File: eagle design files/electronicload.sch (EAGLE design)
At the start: 31 parts, among them Q1 IRLB3034PbF, U1 ARDUINO_BLUEPILL, U2 MCP6004-I/SL, X1 ED350/2

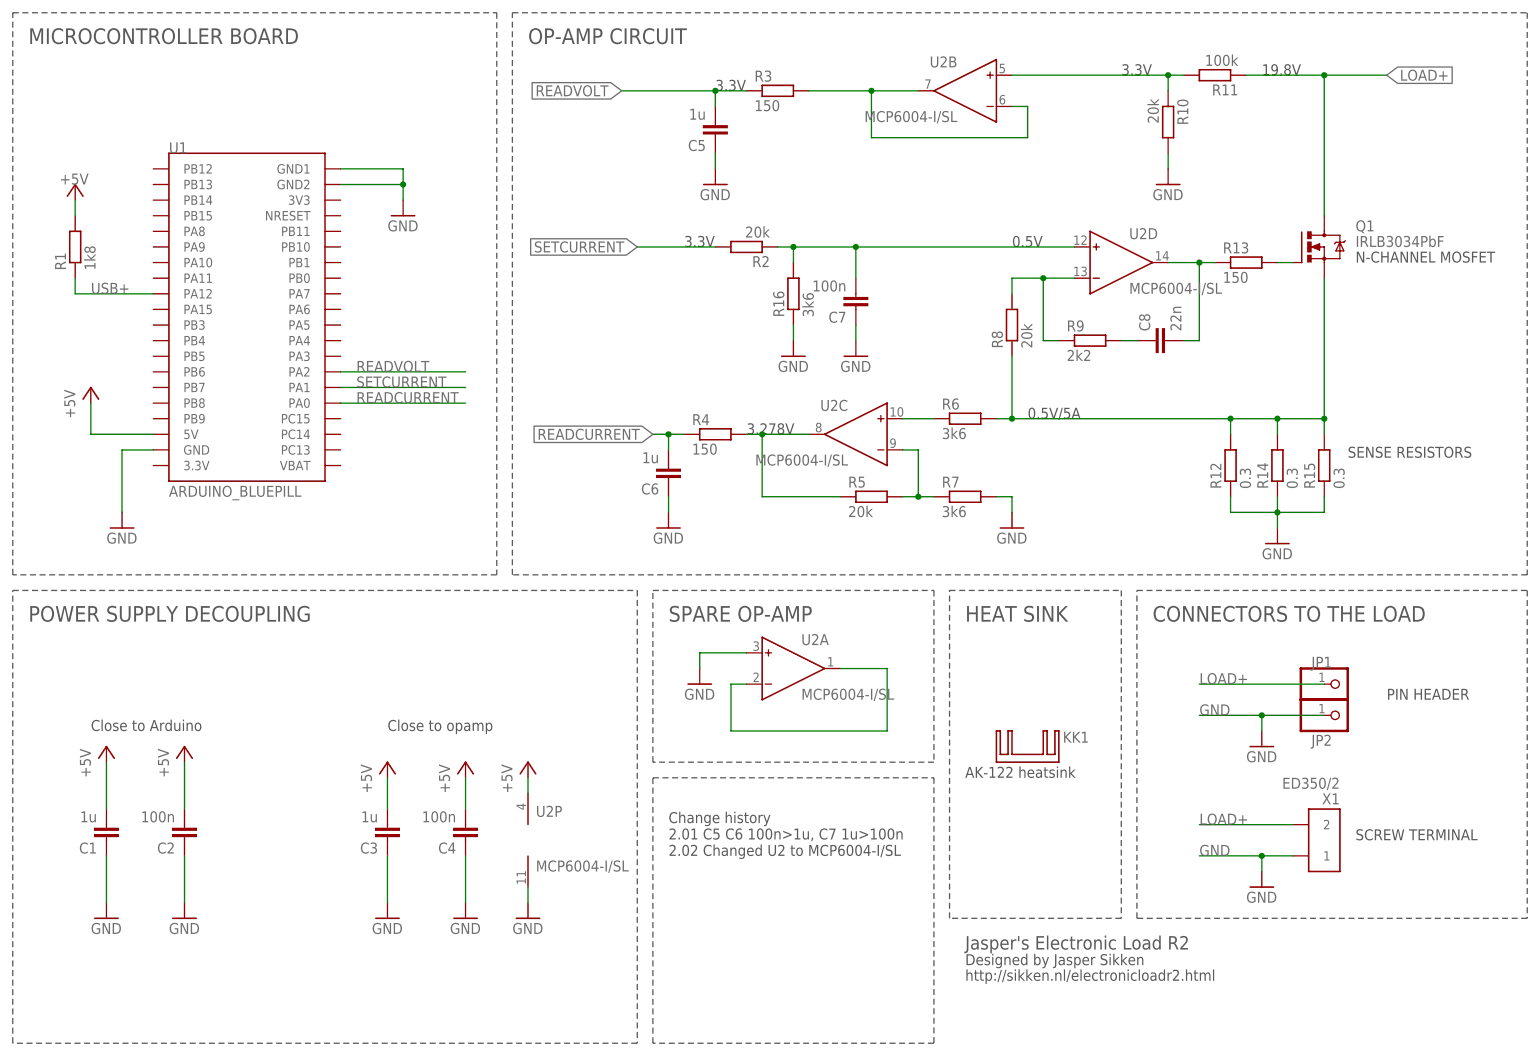
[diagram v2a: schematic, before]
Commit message: 2.03 Changed mosfet to the much more robust BTS133
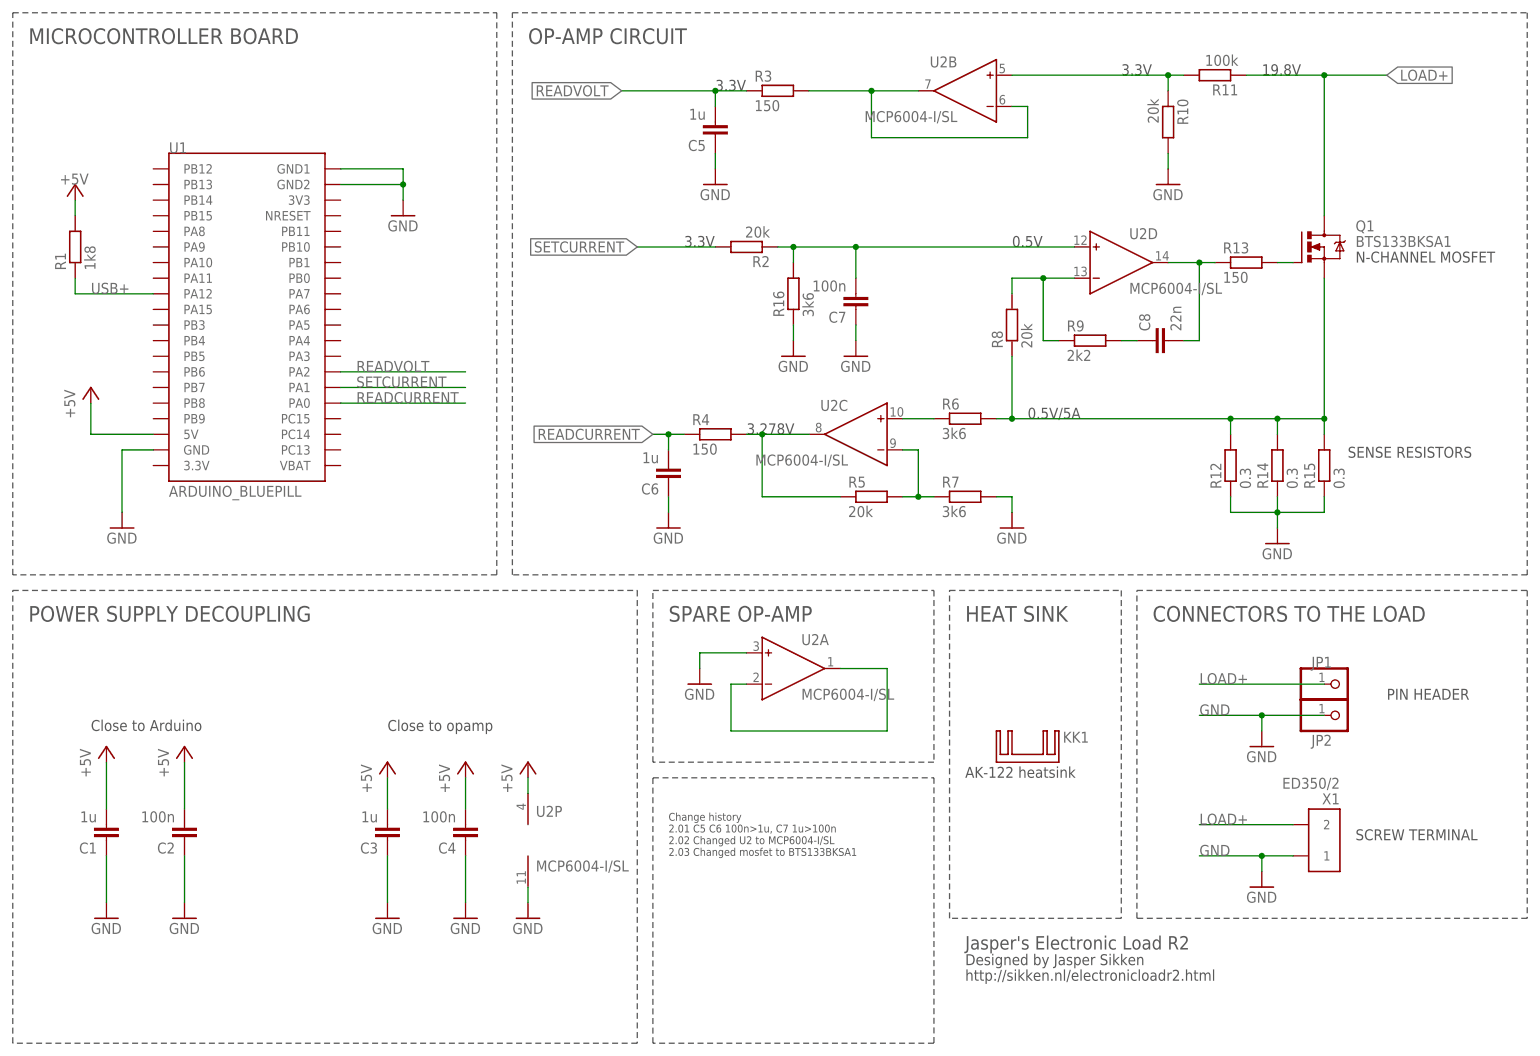
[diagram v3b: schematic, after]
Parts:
- Q1: value IRLB3034PbF -> BTS133BKSA1; DIGIKEY IRLB3034PbF -> BTS133BKSA1-ND; FARNELL_OC (none) -> 2480556; MOUSER_OC (none) -> 726-BTS133BKSA1
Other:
- note added: "Change history 2.01 C5 C6 100n>1u, C7 1u>100n 2.02 Changed U2 to MCP6004-I/SL 2.03 Changed mosfet to BTS133BKSA1"
- note removed: "Change history 2.01 C5 C6 100n>1u, C7 1u>100n 2.02 Changed U2 to MCP6004-I/SL"
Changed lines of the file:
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@@
 <part name="GND3" library="supply1" library_urn="urn:adsk.eagle:library:371" deviceset="GND" device=""/>
 <part name="GND1" library="supply1" library_urn="urn:adsk.eagle:library:371" deviceset="GND" device=""/>
-<part name="Q1" library="electronicload" deviceset="IRLZ44Z" device="" value="IRLB3034PbF">
-<attribute name="DIGIKEY" value="IRLB3034PbF"/>
+<part name="Q1" library="electronicload" deviceset="IRLZ44Z" device="" value="BTS133BKSA1">
+<attribute name="DIGIKEY" value="BTS133BKSA1-ND"/>
+<attribute name="FARNELL_OC" value="2480556"/>
+<attribute name="MOUSER_OC" value="726-BTS133BKSA1"/>
 </part>
 <part name="C5" library="rcl" library_urn="urn:adsk.eagle:library:334" deviceset="C-EU" device="C0603K" package3d_urn="urn:adsk.eagle:package:23680/2" value="1u">
@@
 <text x="162.56" y="48.26" size="1.778" layer="97">AK-122 heatsink</text>
 <text x="162.56" y="20.32" size="2.1844" layer="97">Jasper's Electronic Load R2</text>
-<text x="114.3" y="35.56" size="1.778" layer="97">Change history
+<text x="114.3" y="35.56" size="1.27" layer="97">Change history
 2.01 C5 C6 100n&gt;1u, C7 1u&gt;100n
-2.02 Changed U2 to MCP6004-I/SL</text>
+2.02 Changed U2 to MCP6004-I/SL
+2.03 Changed mosfet to BTS133BKSA1</text>
 <wire x1="111.76" y1="48.26" x2="157.48" y2="48.26" width="0.1524" layer="97" style="shortdash"/>
 <wire x1="157.48" y1="48.26" x2="157.48" y2="5.08" width="0.1524" layer="97" style="shortdash"/>
@@
 </instance>
 <instance part="GND1" gate="1" x="22.86" y="25.4"/>
-<instance part="Q1" gate="G$1" x="218.44" y="134.62"/>
+<instance part="Q1" gate="G$1" x="218.44" y="134.62">
+<attribute name="FARNELL_OC" x="218.44" y="134.62" size="1.778" layer="96" display="off"/>
+<attribute name="MOUSER_OC" x="218.44" y="134.62" size="1.778" layer="96" display="off"/>
+</instance>
 <instance part="C5" gate="G$1" x="121.92" y="152.4" rot="R180">
 <attribute name="DIGIKEY" x="121.92" y="152.4" size="1.778" layer="96" rot="R180" display="off"/>

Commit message: R2.1 New PCB design, added USB connector, changed mosfet from MCP6004 to MCP6074-E/SL
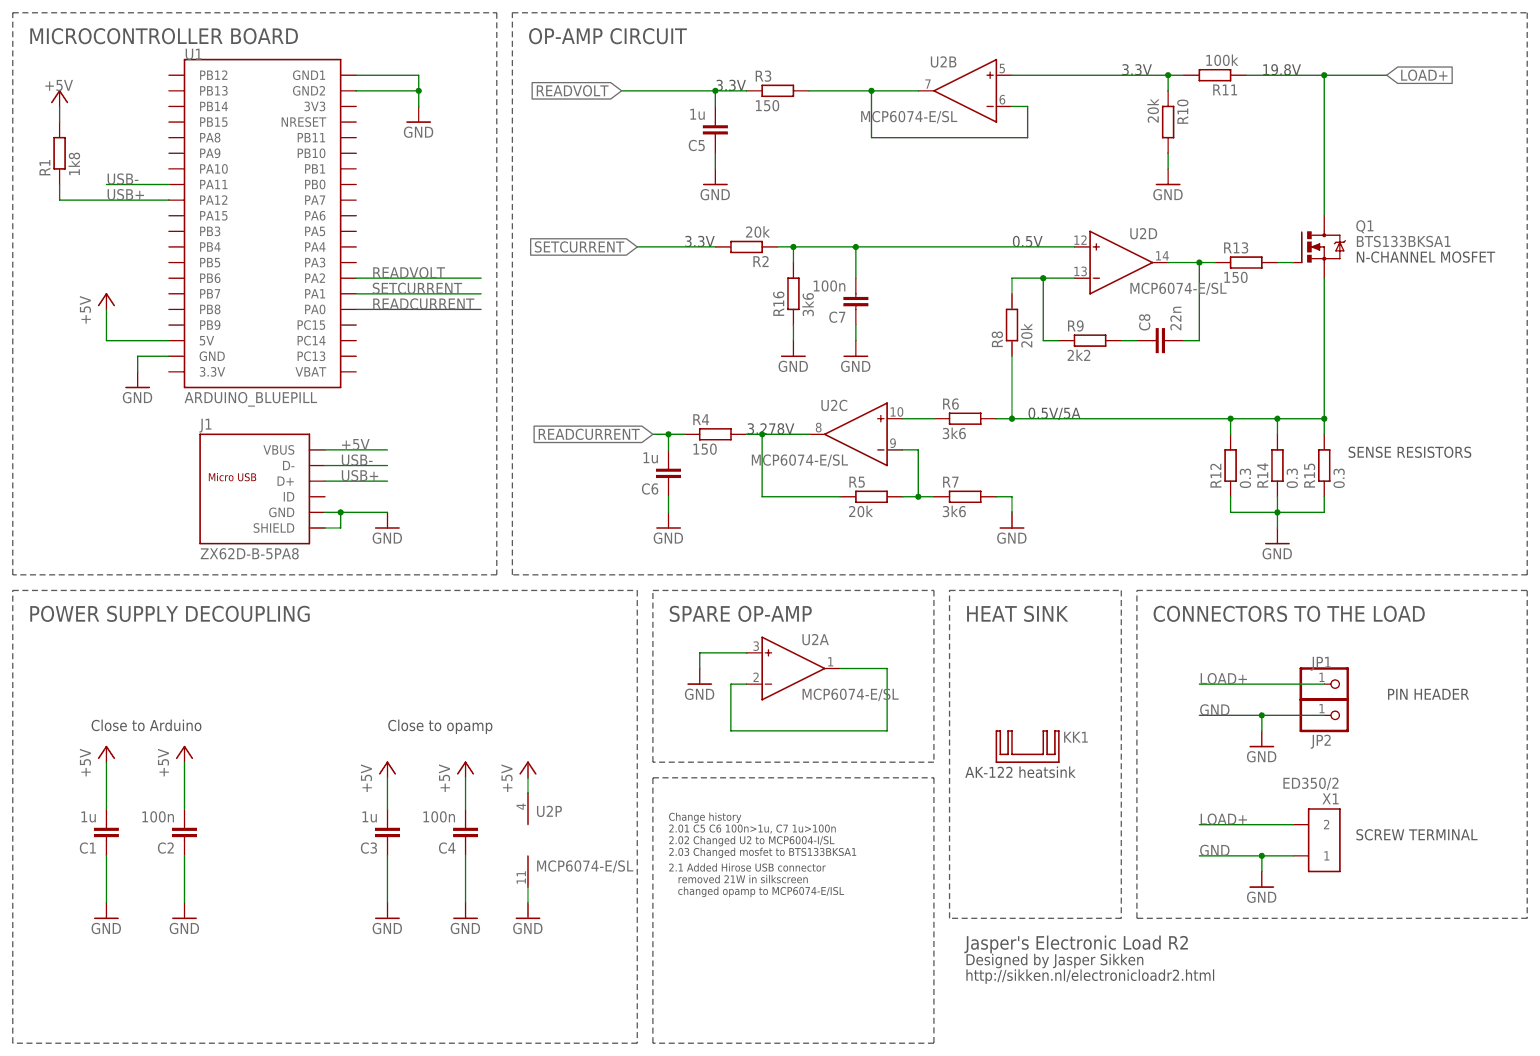
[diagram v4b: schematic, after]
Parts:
- added J1: ZX62D-B-5PA8, sodaq:MICRO-USB-SMD
- U2: value MCP6004-I/SL -> MCP6074-E/SL
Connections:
- new net USB-: J1.D-, U1.PA11
- net +5V: now also J1.VBUS
- net GND: now also J1.GND, J1.SHIELD
- net USB+: now also J1.D+
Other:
- note added: "2.1 Added Hirose USB connector removed 21W in silkscreen changed opamp to MCP6074-E/ISL"
- moved on the sheet: R1, U1
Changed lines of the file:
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@@
 <?xml version="1.0" encoding="utf-8"?>
 <!DOCTYPE eagle SYSTEM "eagle.dtd">
-<eagle version="8.4.1">
+<eagle version="8.5.0">
 <drawing>
 <settings>
@@
 <setting verticaltext="up"/>
 </settings>
-<grid distance="0.1" unitdist="inch" unit="inch" style="lines" multiple="1" display="no" altdistance="0.01" altunitdist="inch" altunit="inch"/>
+<grid distance="0.05" unitdist="inch" unit="inch" style="lines" multiple="1" display="no" altdistance="0.01" altunitdist="inch" altunit="inch"/>
 <layers>
 <layer number="1" name="Top" color="4" fill="1" visible="no" active="no"/>
@@
 <layer number="59" name="tCarbon" color="7" fill="1" visible="no" active="no"/>
 <layer number="60" name="bCarbon" color="7" fill="1" visible="no" active="no"/>
+<layer number="88" name="SimResults" color="9" fill="1" visible="yes" active="yes"/>
+<layer number="89" name="SimProbes" color="9" fill="1" visible="yes" active="yes"/>
 <layer number="90" name="Modules" color="5" fill="1" visible="yes" active="yes"/>
 <layer number="91" name="Nets" color="2" fill="1" visible="yes" active="yes"/>
@@
 <attribute name="DIGIKEY" value="RMCF0603JT20K0CT-ND"/>
 </part>
-<part name="U2" library="electronicload" deviceset="AD8608" device="R" value="MCP6004-I/SL">
+<part name="U2" library="electronicload" deviceset="AD8608" device="R" value="MCP6074-E/SL">
 <attribute name="DIGIKEY" value=""/>
 </part>
@@
 </part>
 <part name="GND17" library="supply1" library_urn="urn:adsk.eagle:library:371" deviceset="GND" device=""/>
+<part name="J1" library="sodaq" deviceset="MICRO-USB-SMD" device="" value="ZX62D-B-5PA8"/>
+<part name="GND18" library="supply1" library_urn="urn:adsk.eagle:library:371" deviceset="GND" device=""/>
 </parts>
 <sheets>
@@
 <wire x1="157.48" y1="5.08" x2="111.76" y2="5.08" width="0.1524" layer="97" style="shortdash"/>
 <wire x1="111.76" y1="5.08" x2="111.76" y2="48.26" width="0.1524" layer="97" style="shortdash"/>
+<text x="114.3" y="29.21" size="1.27" layer="97">2.1 Added Hirose USB connector
+   removed 21W in silkscreen
+   changed opamp to MCP6074-E/ISL</text>
 </plain>
 <instances>
@@
 <instance part="GND16" gate="1" x="210.82" y="30.48"/>
 <instance part="GND15" gate="1" x="210.82" y="53.34"/>
-<instance part="U1" gate="G$1" x="45.72" y="121.92"/>
+<instance part="U1" gate="G$1" x="48.26" y="137.16"/>
 <instance part="R15" gate="G$1" x="220.98" y="99.06" smashed="yes" rot="R90">
 <attribute name="NAME" x="219.4814" y="95.25" size="1.778" layer="95" rot="R90"/>
@@
 <attribute name="VALUE" x="209.042" y="95.25" size="1.778" layer="96" rot="R90"/>
 </instance>
-<instance part="R1" gate="G$1" x="17.78" y="134.62" rot="R90">
-<attribute name="DIGIKEY" x="17.78" y="134.62" size="1.778" layer="96" rot="R90" display="off"/>
-</instance>
-<instance part="P+1" gate="1" x="17.78" y="144.78" smashed="yes">
-<attribute name="VALUE" x="15.24" y="144.78" size="1.778" layer="96"/>
-</instance>
-<instance part="GND2" gate="1" x="25.4" y="88.9"/>
-<instance part="GND7" gate="1" x="71.12" y="139.7"/>
+<instance part="R1" gate="G$1" x="15.24" y="149.86" rot="R90">
+<attribute name="DIGIKEY" x="15.24" y="149.86" size="1.778" layer="96" rot="R90" display="off"/>
+</instance>
+<instance part="P+1" gate="1" x="15.24" y="160.02" smashed="yes">
+<attribute name="VALUE" x="12.7" y="160.02" size="1.778" layer="96"/>
+</instance>
+<instance part="GND2" gate="1" x="27.94" y="111.76"/>
+<instance part="GND7" gate="1" x="73.66" y="154.94"/>
 <instance part="C3" gate="G$1" x="68.58" y="38.1" rot="R180">
 <attribute name="DIGIKEY" x="68.58" y="38.1" size="1.778" layer="96" rot="R180" display="off"/>
@@
 <attribute name="VALUE" x="66.04" y="22.86" size="1.778" layer="96"/>
 </instance>
-<instance part="P+3" gate="1" x="20.32" y="111.76"/>
+<instance part="P+3" gate="1" x="22.86" y="127"/>
 <instance part="R16" gate="G$1" x="134.62" y="127" rot="R90">
 <attribute name="DIGIKEY" x="134.62" y="127" size="1.778" layer="96" rot="R90" display="off"/>
 </instance>
 <instance part="GND17" gate="1" x="134.62" y="116.84"/>
+<instance part="J1" gate="G$1" x="48.26" y="91.44"/>
+<instance part="GND18" gate="1" x="68.58" y="88.9"/>
 </instances>
 <busses>
@@
 <segment>
 <pinref part="U1" gate="G$1" pin="GND"/>
-<wire x1="30.48" y1="101.6" x2="25.4" y2="101.6" width="0.1524" layer="91"/>
+<wire x1="33.02" y1="116.84" x2="27.94" y2="116.84" width="0.1524" layer="91"/>
 <pinref part="GND2" gate="1" pin="GND"/>
-<wire x1="25.4" y1="101.6" x2="25.4" y2="91.44" width="0.1524" layer="91"/>
+<wire x1="27.94" y1="116.84" x2="27.94" y2="114.3" width="0.1524" layer="91"/>
 </segment>
 <segment>
 <pinref part="U1" gate="G$1" pin="GND1"/>
-<wire x1="60.96" y1="147.32" x2="71.12" y2="147.32" width="0.1524" layer="91"/>
+<wire x1="63.5" y1="162.56" x2="73.66" y2="162.56" width="0.1524" layer="91"/>
 <pinref part="GND7" gate="1" pin="GND"/>
-<wire x1="71.12" y1="147.32" x2="71.12" y2="144.78" width="0.1524" layer="91"/>
+<wire x1="73.66" y1="162.56" x2="73.66" y2="160.02" width="0.1524" layer="91"/>
 <pinref part="U1" gate="G$1" pin="GND2"/>
-<wire x1="71.12" y1="144.78" x2="71.12" y2="142.24" width="0.1524" layer="91"/>
-<wire x1="60.96" y1="144.78" x2="71.12" y2="144.78" width="0.1524" layer="91"/>
-<junction x="71.12" y="144.78"/>
+<wire x1="73.66" y1="160.02" x2="73.66" y2="157.48" width="0.1524" layer="91"/>
+<wire x1="63.5" y1="160.02" x2="73.66" y2="160.02" width="0.1524" layer="91"/>
+<junction x="73.66" y="160.02"/>
 </segment>
 <segment>
@@
 <wire x1="134.62" y1="121.92" x2="134.62" y2="119.38" width="0.1524" layer="91"/>
 </segment>
+<segment>
+<pinref part="J1" gate="G$1" pin="GND"/>
+<wire x1="58.42" y1="91.44" x2="60.96" y2="91.44" width="0.1524" layer="91"/>
+<pinref part="J1" gate="G$1" pin="SHIELD"/>
+<wire x1="58.42" y1="88.9" x2="60.96" y2="88.9" width="0.1524" layer="91"/>
+<wire x1="60.96" y1="88.9" x2="60.96" y2="91.44" width="0.1524" layer="91"/>
+<junction x="60.96" y="91.44"/>
+<pinref part="GND18" gate="1" pin="GND"/>
+<wire x1="60.96" y1="91.44" x2="68.58" y2="91.44" width="0.1524" layer="91"/>
+</segment>
 </net>
 <net name="N$12" class="0">
@@
 <segment>
 <pinref part="U1" gate="G$1" pin="PA1"/>
-<wire x1="60.96" y1="111.76" x2="81.28" y2="111.76" width="0.1524" layer="91"/>
-<label x="63.5" y="111.76" size="1.778" layer="95"/>
+<wire x1="63.5" y1="127" x2="83.82" y2="127" width="0.1524" layer="91"/>
+<label x="66.04" y="127" size="1.778" layer="95"/>
 </segment>
 </net>
@@
 <segment>
 <pinref part="U1" gate="G$1" pin="PA0"/>
-<wire x1="60.96" y1="109.22" x2="81.28" y2="109.22" width="0.1524" layer="91"/>
-<label x="63.5" y="109.22" size="1.778" layer="95"/>
+<wire x1="63.5" y1="124.46" x2="83.82" y2="124.46" width="0.1524" layer="91"/>
+<label x="66.04" y="124.46" size="1.778" layer="95"/>
 </segment>
 </net>
@@
 <segment>
 <pinref part="U1" gate="G$1" pin="PA2"/>
-<wire x1="60.96" y1="114.3" x2="81.28" y2="114.3" width="0.1524" layer="91"/>
-<label x="63.5" y="114.3" size="1.778" layer="95"/>
+<wire x1="63.5" y1="129.54" x2="83.82" y2="129.54" width="0.1524" layer="91"/>
+<label x="66.04" y="129.54" size="1.778" layer="95"/>
 </segment>
 </net>
@@
 <pinref part="P+1" gate="1" pin="+5V"/>
 <pinref part="R1" gate="G$1" pin="2"/>
-<wire x1="17.78" y1="142.24" x2="17.78" y2="139.7" width="0.1524" layer="91"/>
+<wire x1="15.24" y1="157.48" x2="15.24" y2="154.94" width="0.1524" layer="91"/>
 </segment>
 <segment>
@@
 <segment>
 <pinref part="U1" gate="G$1" pin="5V"/>
-<wire x1="30.48" y1="104.14" x2="20.32" y2="104.14" width="0.1524" layer="91"/>
-<wire x1="20.32" y1="104.14" x2="20.32" y2="109.22" width="0.1524" layer="91"/>
+<wire x1="33.02" y1="119.38" x2="22.86" y2="119.38" width="0.1524" layer="91"/>
+<wire x1="22.86" y1="119.38" x2="22.86" y2="124.46" width="0.1524" layer="91"/>
 <pinref part="P+3" gate="1" pin="+5V"/>
+</segment>
+<segment>
+<pinref part="J1" gate="G$1" pin="VBUS"/>
+<wire x1="58.42" y1="101.6" x2="68.58" y2="101.6" width="0.1524" layer="91"/>
+<label x="60.96" y="101.6" size="1.778" layer="95"/>
 </segment>
 </net>
@@
 <pinref part="U1" gate="G$1" pin="PA12"/>
 <pinref part="R1" gate="G$1" pin="1"/>
-<wire x1="30.48" y1="127" x2="17.78" y2="127" width="0.1524" layer="91"/>
-<wire x1="17.78" y1="127" x2="17.78" y2="129.54" width="0.1524" layer="91"/>
-<label x="20.32" y="127" size="1.778" layer="95"/>
-</segment>
-</net>
+<wire x1="33.02" y1="142.24" x2="15.24" y2="142.24" width="0.1524" layer="91"/>
+<wire x1="15.24" y1="142.24" x2="15.24" y2="144.78" width="0.1524" layer="91"/>
+<label x="22.86" y="142.24" size="1.778" layer="95"/>
+</segment>
+<segment>
+<pinref part="J1" gate="G$1" pin="D+"/>
+<wire x1="58.42" y1="96.52" x2="68.58" y2="96.52" width="0.1524" layer="91"/>
+<label x="60.96" y="96.52" size="1.778" layer="95"/>
+</segment>
+</net>
+<net name="USB-" class="0">
+<segment>
+<pinref part="U1" gate="G$1" pin="PA11"/>
+<wire x1="33.02" y1="144.78" x2="22.86" y2="144.78" width="0.1524" layer="91"/>
+<label x="22.86" y="144.78" size="1.778" layer="95"/>
+</segment>
+<segment>
+<pinref part="J1" gate="G$1" pin="D-"/>
+<wire x1="58.42" y1="99.06" x2="68.58" y2="99.06" width="0.1524" layer="91"/>
+<label x="60.96" y="99.06" size="1.778" layer="95"/>
+</segment>
+</net>
